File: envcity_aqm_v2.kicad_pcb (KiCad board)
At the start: 4 copper layers, 110 x 100 mm, 109 parts, among them IC1 DS1307ZN+, J1 217175-0001, J10 Conn_01x03_Male, J11 Conn_01x04_Male, J12 Conn_01x02_Male, J13 Conn_01x02_Male, J14 Micro_SD_Card, J2 Screw_Terminal_01x02, J3 Screw_Terminal_01x02, J4 Conn_01x06_Male, J5 Conn_01x06_Male, J6 Conn_01x06_Male, J7 Conn_01x06_Male, Q1 DMG2301L, Q10 BC808, Q11 BC808, Q12 DMG2301L / DMP2045U, Q13 DMN10H220L, Q14 DMN10H220L, Q2 DMG2301L, Q3 BC808, Q4 BC808, Q5 DMG2301L / DMP2045U, Q6 BC808, Q7 BC808, Q8 DMG2301L, Q9 DMG2301L / DMP2045U, U1 ADS1115IDGS, U2 CD74HC4067M, U3 Heltec_Wifi_LoRa_V2, U4 LM2596S-5, U5 TP4056, U6 MT3608, U7 MT3608, U8 DHT11, Y1 32,768KHz

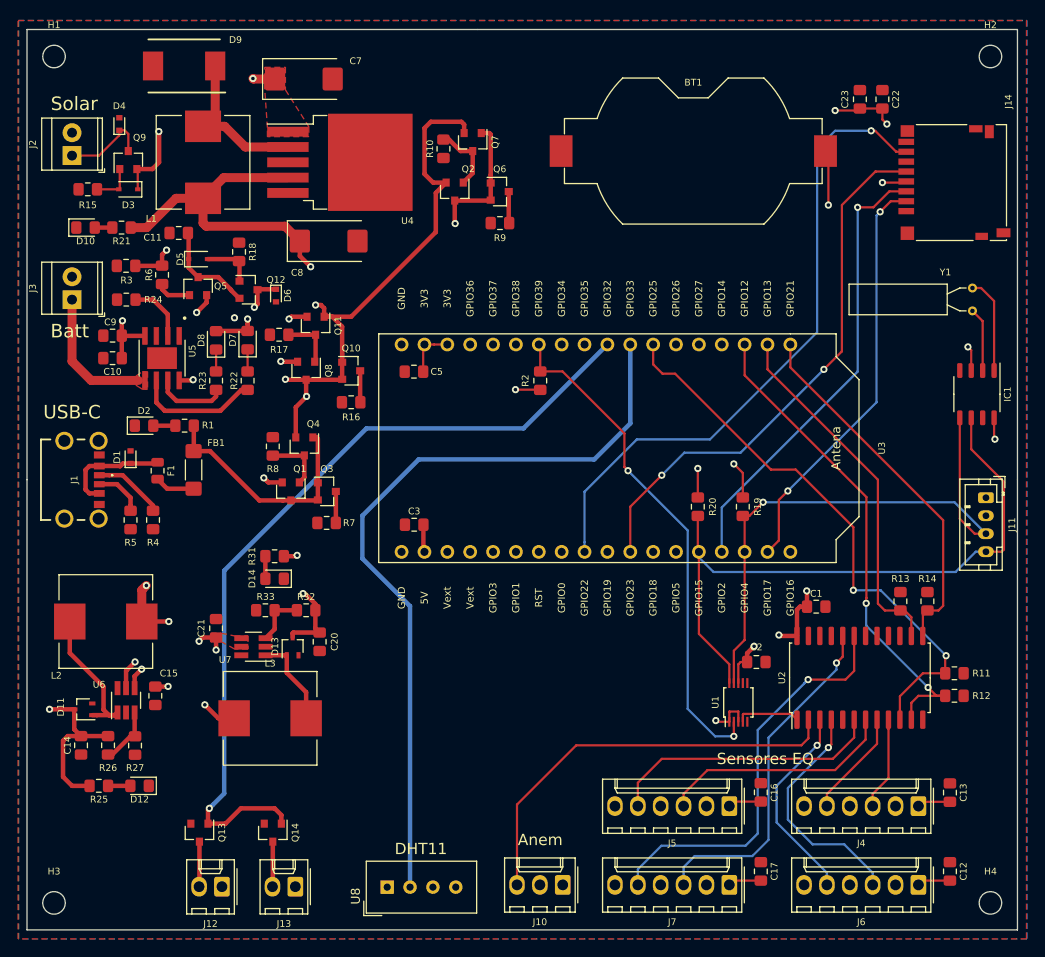
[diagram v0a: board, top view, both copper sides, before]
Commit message: Changing USB conn and add esp32-c3-mini-wroom
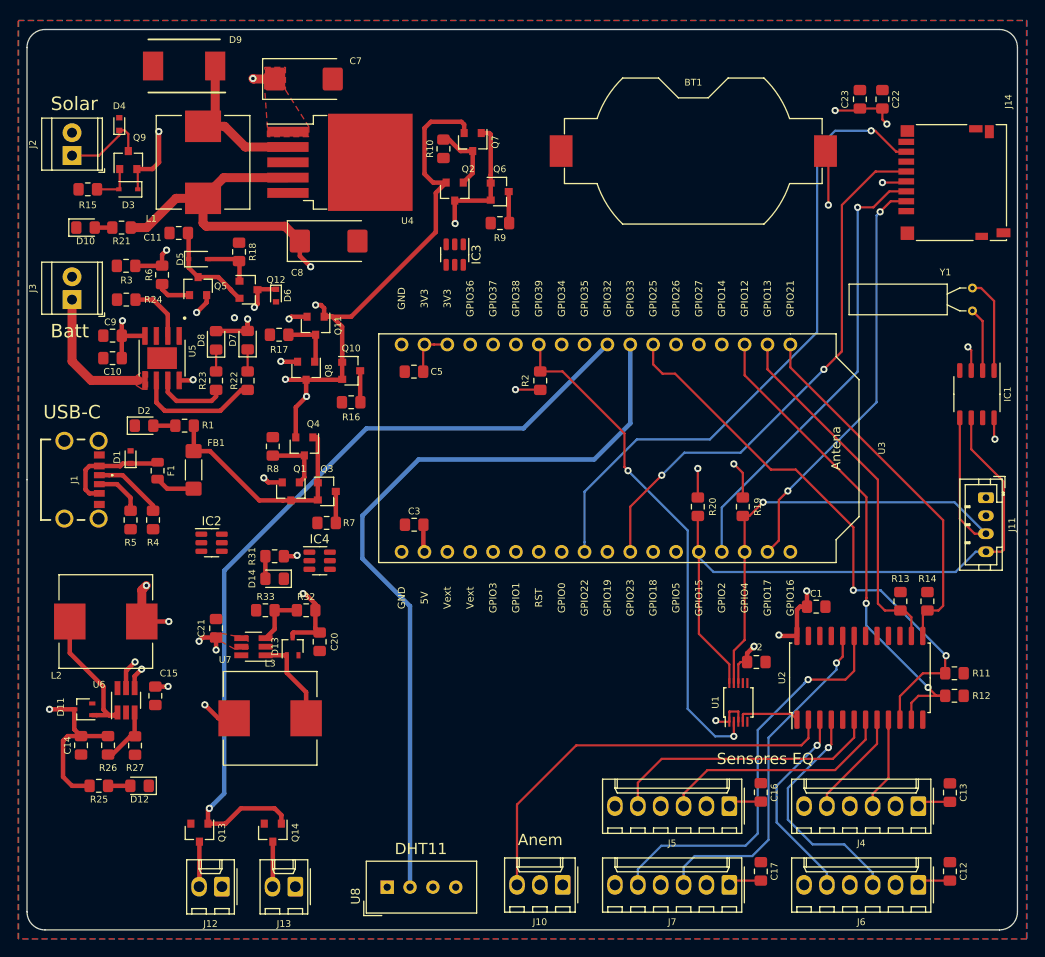
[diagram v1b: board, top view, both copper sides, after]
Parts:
- removed H1, H2, H3, H4: MountingHole, MountingHole:MountingHole_2.5mm
- added IC2: DMMT5401-7F, Package_TO_SOT_SMD:SOT-23-6, F.Cu at (132.0, 117.0)
- added IC3: DMMT5401-7F, Package_TO_SOT_SMD:SOT-23-6, F.Cu at (159.0, 85.0)
- added IC4: DMMT5401-7-F, Package_TO_SOT_SMD:SOT-23-6, F.Cu at (144.0, 119.0)
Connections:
- D11 pad 2: (no net) -> unconnected-(D11-NC-Pad2)
- D13 pad 2: (no net) -> unconnected-(D13-NC-Pad2)
- IC1 pad 7: (no net) -> unconnected-(IC1-SQW/OUT-Pad7)
- J1 pad MH1: (no net) -> unconnected-(J1-PadMH1)
- J1 pad MH2: (no net) -> unconnected-(J1-PadMH2)
- J1 pad MH3: (no net) -> unconnected-(J1-PadMH3)
- J1 pad MH4: (no net) -> unconnected-(J1-PadMH4)
- J14 pad 1: (no net) -> /SD_Data2
- J14 pad 8: (no net) -> /SD_Data1
- Q1 pad 1: Net-(Q1-Pad1) -> Net-(IC2B-C)
- Q2 pad 1: Net-(Q2-Pad1) -> Net-(IC3B-C)
- Q8 pad 1: Net-(Q11-Pad3) -> Net-(IC4B-C)
- R10 pad 1: Net-(Q2-Pad1) -> Net-(IC3B-C)
- R16 pad 1: Net-(Q10-Pad3) -> Net-(IC4A-C)
- R17 pad 1: Net-(Q11-Pad3) -> Net-(IC4B-C)
- R7 pad 1: Net-(Q3-Pad3) -> Net-(IC2A-C)
- R8 pad 1: Net-(Q1-Pad1) -> Net-(IC2B-C)
- R9 pad 1: Net-(Q6-Pad3) -> Net-(IC3A-C)
- U1 pad 5: (no net) -> /AIN1
- U1 pad 6: (no net) -> /AIN2
- U1 pad 7: (no net) -> /AIN3
- U2 pad 16: (no net) -> /I15
- U2 pad 17: (no net) -> /I14
- U2 pad 18: (no net) -> /I13
- U2 pad 21: (no net) -> /I10
- U2 pad 22: (no net) -> /I9
- U2 pad 23: (no net) -> /I8
- U2 pad 5: (no net) -> /I4
- U3 pad 10: (no net) -> /LORA_MISO
- U3 pad 12: (no net) -> unconnected-(U3-LORA_CS/V_SPI_CLK/GPIO18-Pad12)
- U3 pad 13: (no net) -> unconnected-(U3-LORA_SCK/V_SPI_CS0/GPIO5-Pad13)
- U3 pad 18: (no net) -> unconnected-(U3-OLED_RST/U2_RX/GPIO16-Pad18)
- U3 pad 22: (no net) -> /LORA_RST
- U3 pad 23: (no net) -> /LORA_MOSI
- U3 pad 24: (no net) -> /LORA_DIO0
- U3 pad 28: (no net) -> /LORA_DIO1
- U3 pad 29: (no net) -> /LORA_DIO2
- U3 pad 3: (no net) -> unconnected-(U3-Vext-Pad3)
- U3 pad 31: (no net) -> unconnected-(U3-ADC1_2/GPIO38-Pad31)
- U3 pad 32: (no net) -> unconnected-(U3-ADC1_1/GPIO37-Pad32)
- U3 pad 33: (no net) -> unconnected-(U3-ADC1_0/GPIO36-Pad33)
- U3 pad 4: (no net) -> unconnected-(U3-Vext-Pad4)
- U3 pad 5: (no net) -> unconnected-(U3-U0_RX/GPIO3-Pad5)
- U3 pad 6: (no net) -> unconnected-(U3-U0_TX/GPIO1-Pad6)
- U3 pad 7: (no net) -> unconnected-(U3-RST-Pad7)
- U3 pad 8: (no net) -> unconnected-(U3-PRG_BUTTON/TOUCH1/ADC2_1/GPIO0-Pad8)
- U8 pad 3: (no net) -> unconnected-(U8-NC-Pad3)
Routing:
- net +3V3: track 118.3 -> 26.3 mm
- net +9V: track 89.1 -> 18.6 mm
- net Vsys: track 78.3 -> 28.1 mm
- net Vexternal: track 108.7 -> 68.3 mm
- net Net-(BT1-+): track 31.1 -> 8.91 mm
- net Vbat: track 39.9 -> 19.3 mm
- net Vsolar_reg: track 70.5 -> 52.5 mm
- net Vsolar_protected: track 23.9 -> 11.0 mm
- removed copper zone on PWR, net +5V
- removed copper zone on GND, net GND
- removed copper zone on PWR, net Vsys
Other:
- outline, holes or cut-outs redrawn
- copper layers 4 -> 2
- net class Default removed

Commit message: Add um monte de coisa
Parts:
- removed the C3 at (154.5, 115.0)
- removed the C5 at (154.5, 98.0)
- removed the D1 at (123.0, 107.5)
- removed the D3 at (122.8, 77.8)
- removed F1: Fuse, Fuse:Fuse_0805_2012Metric
- removed FB1: Ferrite_Bead, Inductor_SMD:L_1806_4516Metric_Pad1.57x1.80mm_HandSolder
- removed Q10, Q11: BC808, Package_TO_SOT_SMD:SOT-23
- removed the Q3 at (144.8, 111.3)
- removed the Q4 at (142.3, 106.3)
- removed the Q6 at (164.0, 78.0)
- removed the Q7 at (161.0, 72.5)
- removed the R15 at (118.2, 77.8)
- removed the R19 at (191.0, 113.0)
- removed the R20 at (186.0, 113.0)
- removed R4: 5K1, Resistor_SMD:R_0805_2012Metric_Pad1.15x1.40mm_HandSolder
- removed the R5 at (123.0, 114.5)
- removed the U3 at (178.5, 106.5)
- added AE1: Antenna, Connector_Coaxial:U.FL_Molex_MCRF_73412-0110_Vertical, F.Cu at (36.2, 35.6)
- added C11: 10uF, Capacitor_SMD:C_0805_2012Metric, F.Cu at (50.0, 76.0)
- added C15: 10uF, Capacitor_SMD:C_0603_1608Metric, F.Cu at (47.5, 76.0)
- added C16: 100nF, Capacitor_SMD:C_0603_1608Metric, F.Cu at (42.5, 72.0)
- added C17: 100nF, Capacitor_SMD:C_0805_2012Metric, F.Cu at (138.1, 24.0)
- added C19: 100nF, Capacitor_SMD:C_0805_2012Metric, F.Cu at (211.5, 131.1)
- added C21: 100nF, Capacitor_SMD:C_0805_2012Metric, F.Cu at (138.1, 30.0)
- added C22: 10uF, Capacitor_SMD:C_0805_2012Metric, F.Cu at (49.0, 64.0)
- added C23: 10uF, Capacitor_SMD:C_0805_2012Metric, F.Cu at (46.5, 64.0)
- added C24: 100nF, Capacitor_SMD:C_0805_2012Metric, F.Cu at (42.5, 60.0)
- added C26: 100nF, Capacitor_SMD:C_0805_2012Metric, F.Cu at (211.5, 114.0)
- added C29: 100nF, Capacitor_SMD:C_0805_2012Metric, F.Cu at (142.6, 18.0)
- added C30: 1uF, Capacitor_SMD:C_0805_2012Metric, F.Cu at (142.6, 21.0)
- added C31: 22uF, Capacitor_SMD:C_0805_2012Metric, F.Cu at (142.6, 24.0)
- added C32: 100nF, Capacitor_SMD:C_0805_2012Metric, F.Cu at (142.6, 27.0)
- added C33: 100nF, Capacitor_SMD:C_0805_2012Metric, F.Cu at (142.6, 30.0)
- added C6: 20pF, Capacitor_SMD:C_0603_1608Metric, F.Cu at (139.6, 85.5)
- added C7: 20pF, Capacitor_SMD:C_0603_1608Metric, F.Cu at (139.6, 82.4)
- added D16: LED, LED_SMD:LED_0603_1608Metric, F.Cu at (35.5, 61.8)
- added D7: LED, LED_SMD:LED_0603_1608Metric, F.Cu at (35.5, 73.8)
- added D8: 1N5819, Diode_THT:D_DO-41_SOD81_P10.16mm_Horizontal, F.Cu at (7.92, 25.2)
- added H1: MountingHole, MountingHole:MountingHole_2.5mm, F.Cu at (-57.5, -2.65)
- added H2: MountingHole, MountingHole:MountingHole_2.5mm, F.Cu at (-57.5, 3.90)
- added H3: MountingHole, MountingHole:MountingHole_2.5mm, F.Cu at (-57.5, 10.4)
- added H4: MountingHole, MountingHole:MountingHole_2.5mm, F.Cu at (-57.5, 17.0)
- added IC6: ESP32-S2-SOLO-N4R2, ESP32-S2-SOLO-N4R2:ESP32S2SOLON4R2, F.Cu at (161.0, 74.0)
- added J12: Conn_01x06_Male, Connector_Molex:Molex_KK-254_AE-6410-06A_1x06_P2.54mm_Vertical, F.Cu at (216.5, 130.3)
- added J13: Conn_01x06_Male, Connector_Molex:Molex_KK-254_AE-6410-06A_1x06_P2.54mm_Vertical, F.Cu at (216.5, 113.1)
- added J14: Conn_01x08_Pin, Connector_PinSocket_2.54mm:PinSocket_1x08_P2.54mm_Vertical_SMD_Pin1Left, F.Cu at (27.0, 10.8)
- added J7: Conn_01x06_Pin, Connector_Molex:Molex_KK-254_AE-6410-06A_1x06_P2.54mm_Vertical, F.Cu at (335.1, 132.0)
- added R10: 100k, Resistor_SMD:R_0805_2012Metric, F.Cu at (37.5, 78.0)
- added R22: 10k, Resistor_SMD:R_0805_2012Metric, F.Cu at (38.5, 62.1)
- added R23: 100k, Resistor_SMD:R_0805_2012Metric, F.Cu at (37.5, 66.0)
- added R28: 10k, Resistor_SMD:R_0805_2012Metric, F.Cu at (133.7, 23.8)
- added R29: 10k, Resistor_SMD:R_0805_2012Metric, F.Cu at (133.7, 26.8)
- added R34: 10k, Resistor_SMD:R_0805_2012Metric, F.Cu at (133.7, 29.7)
- added R35: 4K7, Resistor_SMD:R_0805_2012Metric, F.Cu at (133.7, 32.7)
- added R36: 4K7, Resistor_SMD:R_0805_2012Metric, F.Cu at (133.7, 35.6)
- added R6: 0R, Resistor_SMD:R_0603_1608Metric, F.Cu at (142.7, 85.0)
- added R7: 0R, Resistor_SMD:R_0603_1608Metric, F.Cu at (142.7, 83.3)
- added R8: 10k, Resistor_SMD:R_0805_2012Metric, F.Cu at (38.5, 74.1)
- added SW1: RESET, Button_Switch_SMD:SW_SPST_PTS810, F.Cu at (36.5, 25.4)
- added SW2: BOOT, Button_Switch_SMD:SW_SPST_PTS810, F.Cu at (52.5, 44.0)
- added U10: RFM95W-915S2, Connector_JAE:JAE_LY20-16P-DLT1_2x08_P2.00mm_Horizontal, F.Cu at (32.2, 2.33)
- added U2: USBLC6-2SC6, Package_TO_SOT_SMD:SOT-23-6, F.Cu at (122.3, 74.8)
- added U6: AP2112K-3.3, Package_TO_SOT_SMD:SOT-23-5, F.Cu at (42.6, 76.0)
- added U8: AP2112K-3.3, Package_TO_SOT_SMD:SOT-23-5, F.Cu at (42.5, 64.0)
- C1: renamed from C22; footprint Capacitor_SMD:C_0805_2012Metric_Pad1.15x1.40mm_HandSolder -> Capacitor_SMD:C_0805_2012Metric
- C12: renamed from C20; footprint Capacitor_SMD:C_0805_2012Metric_Pad1.15x1.40mm_HandSolder -> Capacitor_SMD:C_0805_2012Metric
- C13: renamed from C14; footprint Capacitor_SMD:C_0805_2012Metric_Pad1.15x1.40mm_HandSolder -> Capacitor_SMD:C_0805_2012Metric
- C18: renamed from C16; footprint Capacitor_SMD:C_0805_2012Metric_Pad1.15x1.40mm_HandSolder -> Capacitor_SMD:C_0805_2012Metric
- C2: renamed from C23; footprint Capacitor_SMD:C_0805_2012Metric_Pad1.15x1.40mm_HandSolder -> Capacitor_SMD:C_0805_2012Metric
- C20: renamed from C12; footprint Capacitor_SMD:C_0805_2012Metric_Pad1.15x1.40mm_HandSolder -> Capacitor_SMD:C_0805_2012Metric
- C25: renamed from C17; footprint Capacitor_SMD:C_0805_2012Metric_Pad1.15x1.40mm_HandSolder -> Capacitor_SMD:C_0805_2012Metric
- C27: renamed from C13; footprint Capacitor_SMD:C_0805_2012Metric_Pad1.15x1.40mm_HandSolder -> Capacitor_SMD:C_0805_2012Metric
- C28: renamed from C1; footprint Capacitor_SMD:C_0805_2012Metric_Pad1.15x1.40mm_HandSolder -> Capacitor_SMD:C_0805_2012Metric
- C3: renamed from C9; footprint Capacitor_SMD:C_0805_2012Metric_Pad1.15x1.40mm_HandSolder -> Capacitor_SMD:C_0805_2012Metric
- C34: renamed from C2; footprint Capacitor_SMD:C_0805_2012Metric_Pad1.15x1.40mm_HandSolder -> Capacitor_SMD:C_0805_2012Metric
- C4: renamed from C10; footprint Capacitor_SMD:C_0805_2012Metric_Pad1.15x1.40mm_HandSolder -> Capacitor_SMD:C_0805_2012Metric
- C5: renamed from C11; footprint Capacitor_SMD:C_0805_2012Metric_Pad1.15x1.40mm_HandSolder -> Capacitor_SMD:C_0805_2012Metric
- C8: renamed from C21; footprint Capacitor_SMD:C_0805_2012Metric_Pad1.15x1.40mm_HandSolder -> Capacitor_SMD:C_0805_2012Metric
- C9: renamed from C15; footprint Capacitor_SMD:C_0805_2012Metric_Pad1.15x1.40mm_HandSolder -> Capacitor_SMD:C_0805_2012Metric
- J1: value 217175-0001 -> USB_B_Micro; footprint SamacSys_Parts:2171750001 -> Connector_USB:USB_Micro-B_Wuerth_629105150521
- R1: renamed from R24; footprint Resistor_SMD:R_0805_2012Metric_Pad1.15x1.40mm_HandSolder -> Resistor_SMD:R_0805_2012Metric
- R11: renamed from R32; footprint Resistor_SMD:R_0805_2012Metric_Pad1.15x1.40mm_HandSolder -> Resistor_SMD:R_0805_2012Metric
- R12: renamed from R33; footprint Resistor_SMD:R_0805_2012Metric_Pad1.15x1.40mm_HandSolder -> Resistor_SMD:R_0805_2012Metric
- R13: renamed from R26; footprint Resistor_SMD:R_0805_2012Metric_Pad1.15x1.40mm_HandSolder -> Resistor_SMD:R_0805_2012Metric
- R14: renamed from R27; footprint Resistor_SMD:R_0805_2012Metric_Pad1.15x1.40mm_HandSolder -> Resistor_SMD:R_0805_2012Metric
- R15: renamed from R7; footprint Resistor_SMD:R_0805_2012Metric_Pad1.15x1.40mm_HandSolder -> Resistor_SMD:R_0805_2012Metric
- R16: renamed from R21; footprint Resistor_SMD:R_0805_2012Metric_Pad1.15x1.40mm_HandSolder -> Resistor_SMD:R_0805_2012Metric
- R17: renamed from R31; footprint Resistor_SMD:R_0805_2012Metric_Pad1.15x1.40mm_HandSolder -> Resistor_SMD:R_0805_2012Metric
- R18: renamed from R25; footprint Resistor_SMD:R_0805_2012Metric_Pad1.15x1.40mm_HandSolder -> Resistor_SMD:R_0805_2012Metric
- R19: renamed from R8; footprint Resistor_SMD:R_0805_2012Metric_Pad1.15x1.40mm_HandSolder -> Resistor_SMD:R_0805_2012Metric
- R2: renamed from R22; footprint Resistor_SMD:R_0805_2012Metric_Pad1.15x1.40mm_HandSolder -> Resistor_SMD:R_0805_2012Metric
- R20: renamed from R9; footprint Resistor_SMD:R_0805_2012Metric_Pad1.15x1.40mm_HandSolder -> Resistor_SMD:R_0805_2012Metric
- R21: renamed from R10; footprint Resistor_SMD:R_0805_2012Metric_Pad1.15x1.40mm_HandSolder -> Resistor_SMD:R_0805_2012Metric
- R24: renamed from R16; footprint Resistor_SMD:R_0805_2012Metric_Pad1.15x1.40mm_HandSolder -> Resistor_SMD:R_0805_2012Metric
- R25: renamed from R6; footprint Resistor_SMD:R_0805_2012Metric_Pad1.15x1.40mm_HandSolder -> Resistor_SMD:R_0805_2012Metric
- R26: renamed from R3; footprint Resistor_SMD:R_0805_2012Metric_Pad1.15x1.40mm_HandSolder -> Resistor_SMD:R_0805_2012Metric
- R27: renamed from R17; footprint Resistor_SMD:R_0805_2012Metric_Pad1.15x1.40mm_HandSolder -> Resistor_SMD:R_0805_2012Metric
- R3: renamed from R23; footprint Resistor_SMD:R_0805_2012Metric_Pad1.15x1.40mm_HandSolder -> Resistor_SMD:R_0805_2012Metric
- R30: renamed from R11; footprint Resistor_SMD:R_0805_2012Metric_Pad1.15x1.40mm_HandSolder -> Resistor_SMD:R_0805_2012Metric
- R31: renamed from R12; footprint Resistor_SMD:R_0805_2012Metric_Pad1.15x1.40mm_HandSolder -> Resistor_SMD:R_0805_2012Metric
- R32: renamed from R13; footprint Resistor_SMD:R_0805_2012Metric_Pad1.15x1.40mm_HandSolder -> Resistor_SMD:R_0805_2012Metric
- R33: renamed from R14; footprint Resistor_SMD:R_0805_2012Metric_Pad1.15x1.40mm_HandSolder -> Resistor_SMD:R_0805_2012Metric
- R37: renamed from R2; footprint Resistor_SMD:R_0805_2012Metric_Pad1.15x1.40mm_HandSolder -> Resistor_SMD:R_0805_2012Metric
- R5: renamed from R18; footprint Resistor_SMD:R_0805_2012Metric_Pad1.15x1.40mm_HandSolder -> Resistor_SMD:R_0805_2012Metric
- R9: renamed from R1; footprint Resistor_SMD:R_0805_2012Metric_Pad1.15x1.40mm_HandSolder -> Resistor_SMD:R_0805_2012Metric
- moved C13 228.6 mm to (-106.5, 185.0), turned to 180 degrees
- moved C9 227.2 mm to (-96.8, 180.0)
- moved D15 227.2 mm to (-98.5, 190.0)
- moved L2 227.2 mm to (-102.3, 171.8)
- moved R13 227.2 mm to (-102.0, 185.5)
- moved U4 227.2 mm to (-100.0, 180.5)
- moved R18 227.2 mm to (-103.0, 190.0)
- moved D11 226.9 mm to (-104.6, 180.8), turned to -90 degrees
- moved R14 226.3 mm to (-97.9, 186.2), turned to 0 degrees
- moved R20 215.7 mm to (-45.4, 133.0), turned to 0 degrees
- moved Q4 215.1 mm to (-50.0, 129.0)
- moved C12 214.8 mm to (-65.0, 177.5)
- moved C3 214.8 mm to (-88.0, 143.5)
- moved C4 214.8 mm to (-88.0, 146.0)
- moved C5 214.8 mm to (-80.7, 132.1)
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- renumbered C7 to C10, C8 to C14, D4 to D1, D13 to D10, D9 to D12, D10 to D13, D12 to D15, D6 to D2, D7 to D3, D8 to D4, D5 to D6, D2 to D9, J6 to J10, J7 to J11, J12 to J15, J13 to J16, J14 to J4, J10 to J5, J11 to J6, J4 to J8, J5 to J9, L3 to L1, L1 to L3, Q9 to Q1, Q12 to Q2, Q1 to Q3, Q2 to Q4, Q8 to Q6, Q13 to Q7, Q14 to Q8, U5 to U1, U1 to U11, U7 to U3, U6 to U4, U4 to U5, U8 to U7, U2 to U9
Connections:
- net /ADS_SCL renamed /SCL
- net /ADS_SDA renamed /SDA
- net Net-(U4-OUT) renamed /out_LM2596S
- net Vsolar renamed /Vsolar
- J10 pad 3: /I5 -> /I4
- J10 pad 5: /I6 -> /I5
- J11 pad 3: /I11 -> /I6
- J11 pad 5: /I12 -> /I7
- J4 pad 1: /SD_Data2 -> unconnected-(J4-DAT2-Pad1)
- J4 pad 5: /SD_CLK -> /SD_SCK
- J4 pad 8: /SD_Data1 -> unconnected-(J4-DAT1-Pad8)
- Q1 pad 1: Net-(D3-A) -> GND
- Q8 pad 1: /FAN1 -> /FAN2
- U7 pad 2: /DHT11 -> /DHT_PIN
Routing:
- net /FAN1: track 91.9 -> 0.00 mm, vias 1 -> 0
- net /DHT11: track 86.2 -> 0.00 mm
- net /SCL: track 72.3 -> 0.00 mm
- net /SD_MISO: track 71.9 -> 0.00 mm, vias 1 -> 0
- net /SDA: track 63.0 -> 0.00 mm, vias 1 -> 0
- net /S0: track 62.9 -> 0.00 mm, vias 2 -> 0
- net /SD_CLK: track 60.6 -> 0.00 mm, vias 2 -> 0
- net Vexternal: track 68.3 -> 9.26 mm, vias 6 -> 0
- net /S1: track 54.8 -> 0.00 mm, vias 2 -> 0
- net /ADS_ALERT: track 56.8 -> 3.77 mm, vias 2 -> 0
- net /SD_MOSI: track 50.7 -> 0.00 mm, vias 1 -> 0
- net /I7: track 46.4 -> 0.00 mm
- net /SD_CS: track 46.3 -> 0.00 mm, vias 2 -> 0
- net /I12: track 46.1 -> 0.00 mm, vias 1 -> 0
- net +5V: track 55.3 -> 12.9 mm, vias 8 -> 0
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- added copper zone on F.Cu, net +5V
- added copper zone on F.Cu, net /BST_FB_9V
- added copper zone on F.Cu, net /out_LM2596S
- added copper zone on F.Cu, net Vsolar_reg
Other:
- board text added: "Battery"
- board text added: "USB"
- board text removed: "Batt"
- board text removed: "USB-C"

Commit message: Add diversas trilhas e corrige 3dmodel
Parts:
- C34: footprint Capacitor_SMD:C_0805_2012Metric -> Capacitor_SMD:C_0603_1608Metric
- J14: footprint Connector_PinSocket_2.54mm:PinSocket_1x08_P2.54mm_Vertical_SMD_Pin1Left -> Connector_PinHeader_2.54mm:PinHeader_1x08_P2.54mm_Vertical
- R25, R26, R30, R31, R32, R33, R37: footprint Resistor_SMD:R_0805_2012Metric -> Resistor_SMD:R_0603_1608Metric
- U10: footprint Connector_JAE:JAE_LY20-16P-DLT1_2x08_P2.00mm_Horizontal -> RF_Module:HOPERF_RFM9XW_SMD
- moved R18 286.1 mm to (170.2, 105.2), turned to 90 degrees
- moved D15 283.2 mm to (170.2, 100.7), turned to -90 degrees
- moved C13 282.2 mm to (165.2, 108.8), turned to -90 degrees
- moved R13 279.8 mm to (165.7, 104.2), turned to 0 degrees
- moved R14 278.0 mm to (166.4, 100.1), turned to 90 degrees
- moved D11 275.7 mm to (161.0, 106.8), turned to 0 degrees
- moved U4 272.2 mm to (160.7, 102.2), turned to 180 degrees
- moved C12 270.3 mm to (185.6, 76.2)
- moved C8 270.3 mm to (174.1, 74.8)
- moved D10 270.3 mm to (182.6, 76.8)
- moved D14 270.3 mm to (192.3, 76.1)
- moved L1 270.3 mm to (180.1, 84.8)
- moved R11 270.3 mm to (184.1, 72.8)
- moved R12 270.3 mm to (179.6, 72.8)
- moved R17 270.3 mm to (189.8, 76.3)
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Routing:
- net D+: track 23.4 -> 0.00 mm
- net D-: track 22.6 -> 0.00 mm
- net +5V: track 12.9 -> 35.1 mm
- net Vexternal: track 9.26 -> 29.3 mm, vias 0 -> 6
- net /BST_SW_9V: track 12.8 -> 0.00 mm
- net +3V3: track 0.00 -> 12.5 mm
- net Net-(U1-~{STDBY}): track 15.5 -> 3.79 mm
- net /Vsolar: track 11.1 -> 0.00 mm
- net ESP_USB_D-: track 9.42 -> 0.00 mm
- net 3V3-RFM: track 0.00 -> 8.53 mm
- net ESP_USB_D+: track 8.85 -> 0.35 mm
- net Net-(IC3B-C): track 0.00 -> 7.93 mm
- net Vsolar_reg: track 32.5 -> 25.2 mm
- net /AIN0: track 0.00 -> 6.91 mm
- net Vbat_protected: track 5.40 -> 11.2 mm
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- added copper zone on B.Cu, net Vexternal
- removed copper zone on F.Cu, net /BST_FB_9V
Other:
- board size 110 x 100 mm -> 100 x 100 mm
- board text added: "CHRG"
- board text added: "STDBY"
- board text added: "USB2.0"

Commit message: circuito esp32 ok
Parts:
- removed D10: BAT54W, Package_TO_SOT_SMD:SOT-323_SC-70
- added D5: BAT54W, Diode_SMD:D_SOD-123, F.Cu at (159.7, 107.5)
- C29, C30, C31, C33: footprint Capacitor_SMD:C_0805_2012Metric -> Capacitor_SMD:C_0603_1608Metric
- D11: footprint Package_TO_SOT_SMD:SOT-323_SC-70 -> Diode_SMD:D_SOD-123
- R34: footprint Resistor_SMD:R_0805_2012Metric -> Resistor_SMD:R_0603_1608Metric
- moved AE1 174.2 mm to (208.0, 64.0)
- moved SW2 125.6 mm to (176.8, 62.2), turned to 180 degrees
- moved SW1 109.6 mm to (139.8, 62.2)
- moved C32 68.9 mm to (200.0, 65.0), turned to 90 degrees
- moved J4 63.5 mm to (189.0, 26.6)
- moved C29 57.2 mm to (144.8, 75.1), turned to -90 degrees
- moved C30 54.3 mm to (146.8, 75.1), turned to -90 degrees
- moved C12 53.2 mm to (176.1, 128.6), turned to 0 degrees
- moved R11 52.2 mm to (175.2, 124.2), turned to 90 degrees
- moved R12 47.1 mm to (175.2, 119.7), turned to 90 degrees
- moved C31 45.3 mm to (145.2, 69.2), turned to 90 degrees
- moved R34 44.5 mm to (146.0, 72.5)
- moved U3 42.2 mm to (171.2, 118.3), turned to 90 degrees
- moved C33 39.6 mm to (148.0, 69.2), turned to 90 degrees
- moved C8 39.5 mm to (173.2, 114.2), turned to 0 degrees
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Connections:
- net Net-(AE1-A) renamed /ANT
- D11 pad 1: /BST_SW_9V -> +5V
- D11 pad 2: unconnected-(D11-NC-Pad2) -> /BST_SW_5V
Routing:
- net Vsolar_reg: track 25.2 -> 63.0 mm, vias 0 -> 2
- net Net-(IC6-IO0): track 0.00 -> 30.6 mm, vias 0 -> 2
- net /EN: track 0.00 -> 29.1 mm, vias 0 -> 2
- net +3V3: track 12.5 -> 22.1 mm
- net /BST_SW_5V: track 10.2 -> 19.6 mm
- net /ANT: track 0.00 -> 3.97 mm
- net 3V3-RFM: track 8.53 -> 12.1 mm
- net +9V: track 13.0 -> 15.5 mm
- net +5V: track 35.1 -> 37.2 mm
- added copper zone on F.Cu, net /BST_SW_9V
- removed copper zone on F.Cu, net +5V

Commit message: Alterando os indutores. Add diversos 3dmodel. Alterando cristal rtc. Refaz algumas trilhas
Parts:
- removed D8: 1N5819, Diode_THT:D_DO-41_SOD81_P10.16mm_Horizontal
- removed Y1: 32,768KHz, Crystal:Crystal_AT310_D3.0mm_L10.0mm_Horizontal
- added Y2: AB26TRB, AB26TRB-32.768KHZ-T:XTAL_AB26TRB-32.768KHZ-T, F.Cu at (170.8, 105.4)
- C1, C2: footprint Capacitor_SMD:C_0805_2012Metric -> Capacitor_SMD:C_0603_1608Metric
- D12: footprint SamacSys_Parts:DIOM8059X256N -> Diode_SMD:D_SMB
- L1, L2: value 4.7 to 22uH -> XR0530-100M; footprint Inductor_SMD:L_Wuerth_HCI-1040 -> Inductor_SMD:L_Chilisin_BMRA00050530
- L3: value 33uH -> FAUL0630-330MT; footprint Inductor_SMD:L_Wuerth_HCI-1040 -> FDSD0630-H-1R0M_P3:IND_FDSD0630-H-1R0M=P3
- R11, R12, R35, R36: footprint Resistor_SMD:R_0805_2012Metric -> Resistor_SMD:R_0603_1608Metric
- moved U7 117.3 mm to (69.7, 50.5)
- moved C11 102.8 mm to (127.2, 50.2)
- moved C15 102.8 mm to (124.5, 50.0)
- moved C16 102.8 mm to (119.8, 46.1)
- moved D7 102.8 mm to (113.2, 48.1)
- moved R10 102.8 mm to (114.8, 52.1)
- moved R8 102.8 mm to (115.8, 48.2)
- moved U6 102.8 mm to (119.9, 50.2)
- moved D5 102.1 mm to (58.0, 98.8)
- moved C13 102.1 mm to (63.5, 100.1)
- moved C9 102.1 mm to (58.5, 90.3)
- moved D15 102.1 mm to (68.5, 92.1)
- moved R13 102.1 mm to (64.0, 95.6)
- moved R14 102.1 mm to (64.8, 91.4)
- moved R18 102.1 mm to (68.5, 96.6)
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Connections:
- IC2 pad 2: Vusb_protected -> Vusb
- IC2 pad 3: Vusb_protected -> Vusb
- IC2 pad 6: Vusb_protected -> Vusb
- Q3 pad 3: Vusb_protected -> Vusb
- R9 pad 1: Vusb_protected -> Vusb
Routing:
- net +3V3: track 22.1 -> 68.4 mm, vias 0 -> 4
- net Vsolar_reg: track 63.0 -> 36.0 mm, vias 2 -> 1
- net Net-(IC6-IO0): track 30.6 -> 46.1 mm
- net /BST_SW_5V: track 19.6 -> 4.12 mm
- net /out_LM2596S: track 0.00 -> 15.3 mm
- net Net-(BT1-+): track 0.00 -> 11.2 mm
- net Vusb_protected: track 8.41 -> 0.00 mm
- net Vusb: track 8.67 -> 16.0 mm
- net /SCL: track 0.00 -> 5.41 mm
- net +5V: track 37.2 -> 42.5 mm
- net /SDA: track 0.00 -> 5.18 mm
- net Net-(IC1-X2): track 0.00 -> 3.41 mm
- net Net-(IC1-X1): track 0.00 -> 3.40 mm
- net /EN: track 29.1 -> 32.5 mm
- net /BST_FB_5V: track 6.17 -> 9.07 mm
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- added copper zone on F.Cu, net /BST_SW_5V
- removed copper zone on F.Cu, net /BST_SW_9V
- removed copper zone on F.Cu, net /out_LM2596S

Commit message: Roteamento do cartao sd (incompleto). Roteamento USB com controle de impedancia ok.
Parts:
- U9: value CD74HC4067M -> 74HC4067DB; footprint Package_SO:SOIC-24W_7.5x15.4mm_P1.27mm -> Package_SO:SSOP-24_5.3x8.2mm_P0.65mm
- moved J4 105.6 mm to (132.4, 66.8)
- moved C2 100.3 mm to (140.8, 68.4), turned to 90 degrees
- moved C1 99.1 mm to (142.6, 68.4), turned to 90 degrees
- moved J7 79.0 mm to (256.2, 135.0)
- moved SW2 33.7 mm to (115.6, 88.4), turned to 0 degrees
- moved IC1 30.1 mm to (194.0, 116.3), turned to 0 degrees
- moved R17 26.0 mm to (153.2, 108.5)
- moved D14 26.0 mm to (155.7, 108.3)
- moved D11 19.5 mm to (159.6, 106.4)
- moved C12 19.5 mm to (165.4, 106.6)
- moved C8 19.5 mm to (164.6, 94.8)
- moved L1 19.5 mm to (158.0, 100.3)
- moved R11 19.5 mm to (167.8, 98.6)
- moved R12 19.5 mm to (167.8, 94.8)
- moved U3 19.5 mm to (163.6, 100.4)
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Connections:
- IC6 pad 10: /SD_CS -> /SD_SCK
- IC6 pad 11: /SD_SCK -> /SD_MISO
- IC6 pad 18: /RFM_MISO -> /RFM_CS
- IC6 pad 20: /RFM_SCK -> /RFM_MISO
- IC6 pad 21: /RFM_CS -> /RFM_SCK
- IC6 pad 8: /SD_MOSI -> /SD_CS
- IC6 pad 9: /SD_MISO -> /SD_MOSI
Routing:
- net /SD_MISO: track 0.00 -> 28.9 mm
- net D+: track 0.00 -> 27.3 mm
- net D-: track 0.00 -> 27.2 mm
- net /SD_SCK: track 0.00 -> 26.0 mm
- net /SD_MOSI: track 0.00 -> 23.1 mm
- net /SD_CS: track 0.00 -> 20.7 mm, vias 0 -> 2
- net Net-(IC6-IO0): track 46.1 -> 65.2 mm
- net Net-(BT1-+): track 11.2 -> 29.1 mm
- net /EN: track 32.5 -> 41.6 mm
- net +3V3: track 68.4 -> 73.5 mm, vias 4 -> 6
- net Vusb: track 16.0 -> 19.9 mm, vias 0 -> 2
- net ESP_USB_D-: track 0.00 -> 3.78 mm
- net ESP_USB_D+: track 0.35 -> 4.08 mm
- net /ADS_ALERT: track 0.00 -> 3.00 mm
- net /S3: track 3.03 -> 4.86 mm
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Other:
- board text added: "USB PWR"
- board text removed: "USB"
